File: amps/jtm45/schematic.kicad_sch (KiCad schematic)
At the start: 62 parts, among them T3 OT

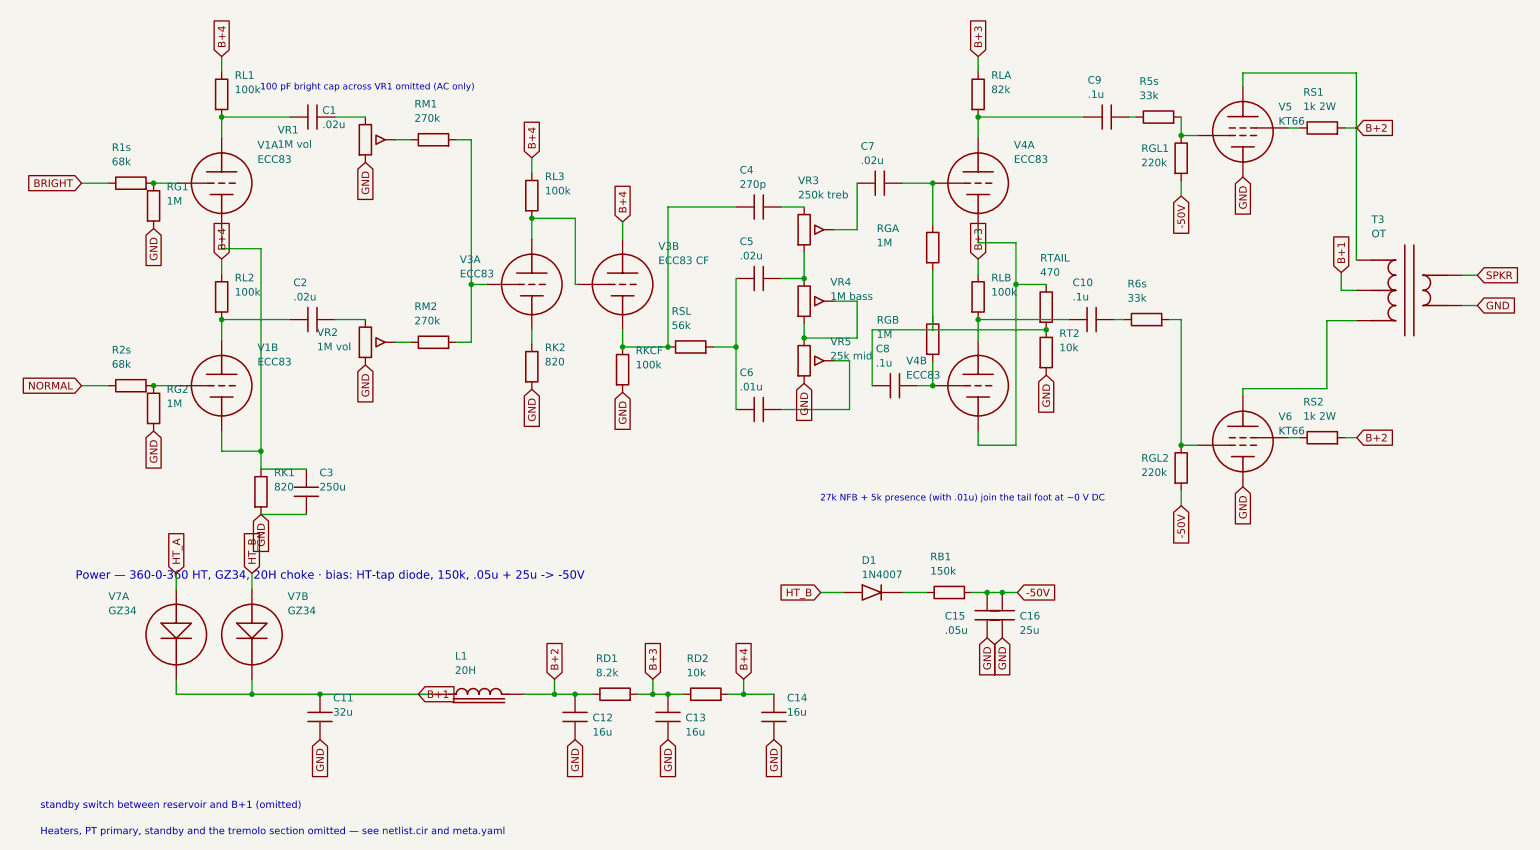
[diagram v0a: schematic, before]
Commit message: Add: real tube pin numbers and readable valve glyphs on every schematic
Phase B of the drawing program. A factory service sheet numbers every tube
pin, because the number is what a technician puts a probe on. This corpus
printed none, and the numbers hidden in its symbols were positional
placeholders (P=1, G=2, K=3) that would have published a 6V6GT's plate as
pin 1 when it is pin 3.

1055 electrodes now carry the real number, 1027 lettered (27 are shared
filaments deduped, 1 dropped for want of clear space on the 6G2). Resolved per
instance from reference/tubes/<slug>.yaml through the same alias resolution the
layout renderer uses, so a 12AX7 section and a 6SL7 section each get their own
basing. A valve whose basing the corpus does not carry prints nothing rather
than a wrong number.

Section letters and basing units are now separate things, which cost a detour
worth recording. The RCA 12AX7-A sheet reads "Pin 1 - Plate of Unit No.2 ...
Pin 6 - Plate of Unit No.1", so unit numbering is not pin order; the 5Y3 and
GZ34 number their units in opposite pin order, so nothing positional can
express it. But the section LETTER is a designator, not a basing fact: this
corpus, like every technician, calls the first stage in signal order V1A, and
five amps' prose already did. On four amps the factory sheets put that first
stage on the other half -- the AA764's own schematic prints +200 V on pin 1 --
so those drawings now state their unit explicitly, each citing its source, and
no letter, netlist, parts list or layout comment changed. 183 layout comments
agree with the printed numbers, 0 disagree. A guard fires if two halves of one
bottle resolve to the same unit, which is exactly how this was found.

Glyphs: the cathode gains a bracket and filament hairpin so it can no longer be
confused with the plate bar, the pentode's screen sits on its own row, and a
rectifier draws as one envelope over its sections instead of two apparent
bottles. Line weights are scaled per sheet to a co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
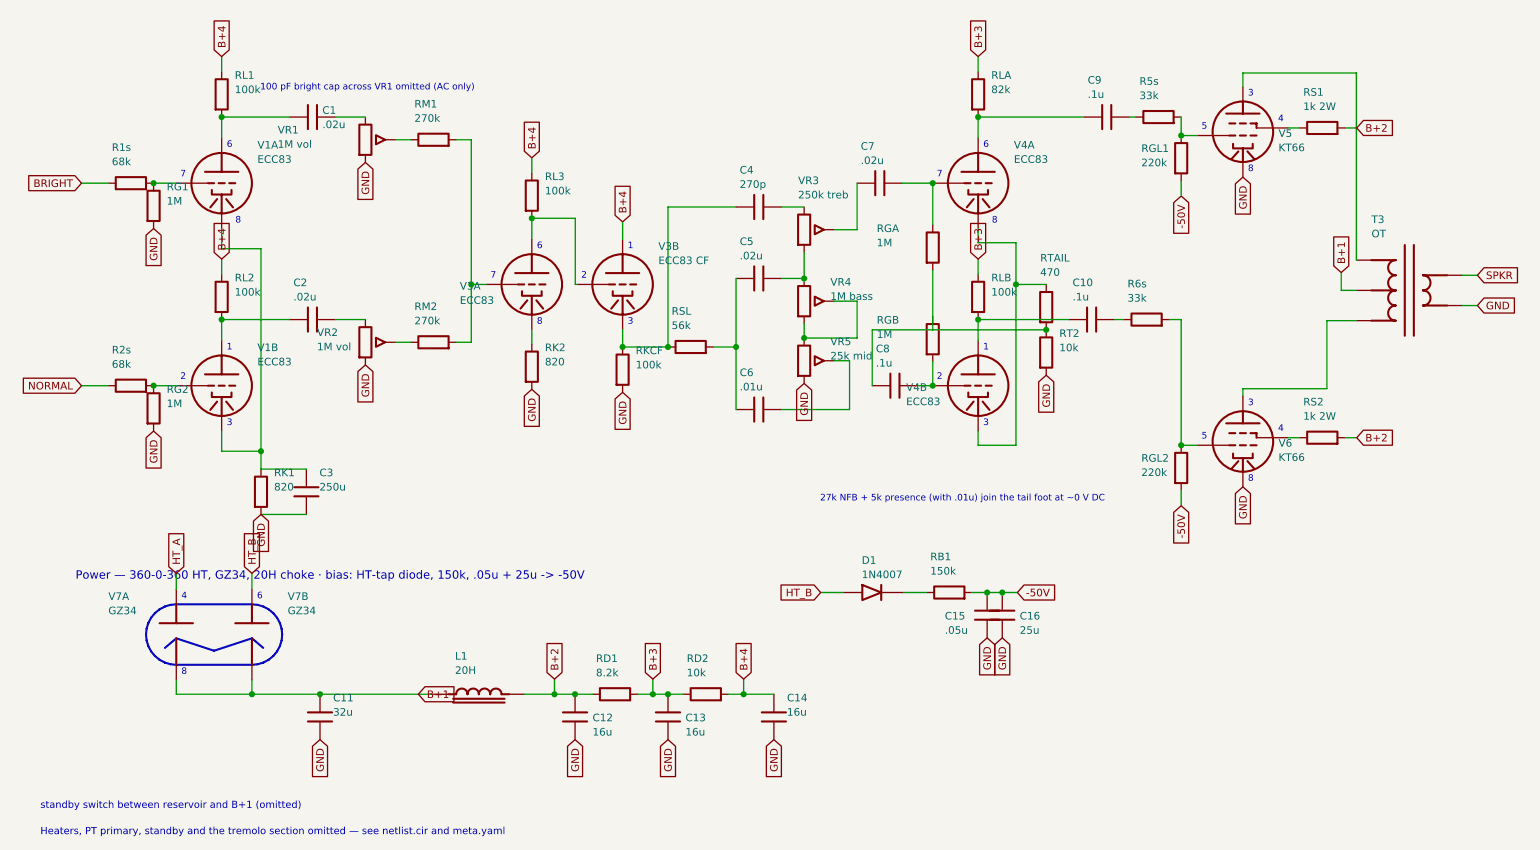
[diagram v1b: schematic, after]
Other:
- note added: "1"
- note added: "2"
- note added: "3"
- note added: "4"
- note added: "5"
- note added: "6"
- note added: "7"
- note added: "8"

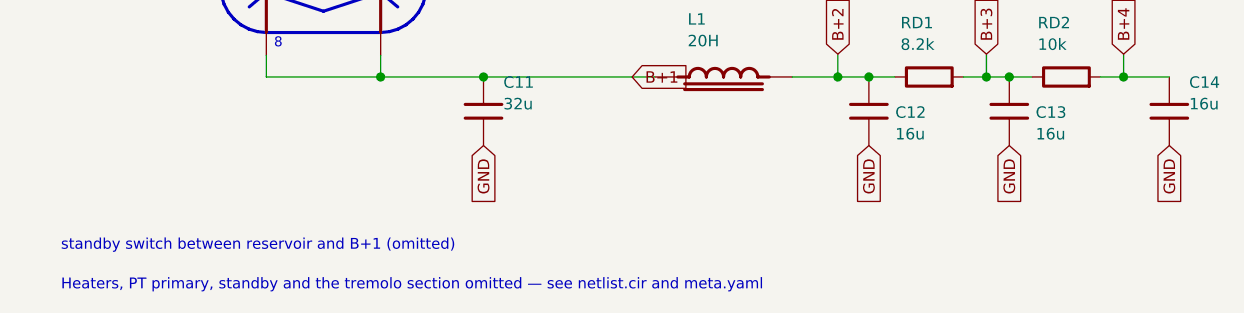
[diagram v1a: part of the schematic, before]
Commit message: Fix: schematic sheet notes no longer name repository files
Thirty-seven committed sheets rendered footnotes and section notes such as
"Heaters and PT primary omitted — see netlist.cir and meta.yaml" or
"excluded from netlist.cir (notes.md)" to visitors through KiCanvas. The
prose sweeps never counted sheets. Rewritten in the site's own words — the
netlist, the sources list, the circuit story, the parts list, the board
drawing — in 59 strings across 33 draw scripts, keeping every technical
claim as it was; the three tone sheets (6G4, 6G5, 6G6-B) are under repair
elsewhere and keep theirs for now. The sweep touched only strings passed to
the sheet's note, text, caption and footnote calls, never a path or a value.

Gates: check_schematics 40/0, connectivity 0 isolated pins;
verify_schematic_nets 40 clean; only the regenerated sheets and their served
copies changed.

Co-Authored-By: Claude Fable 5.1 <noreply@anthropic.com>
Claude-Session: https://claude.ai/code/session_01KBMfdh37HmCL2iWcBiL5J1
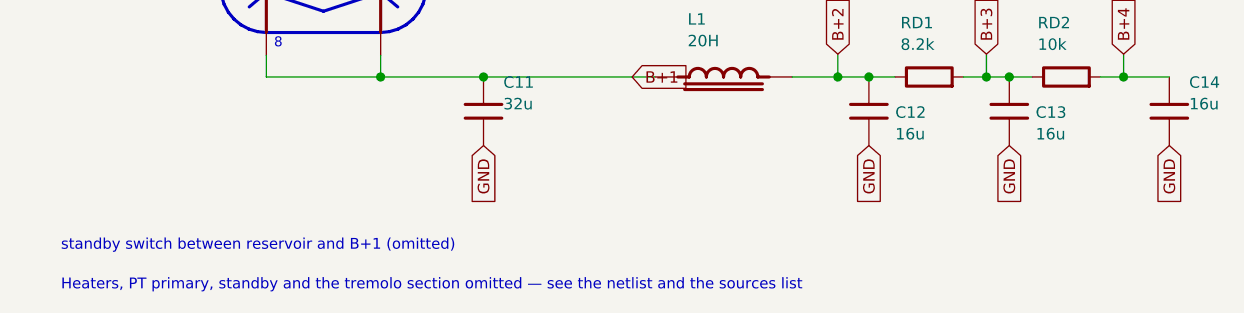
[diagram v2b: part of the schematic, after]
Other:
- note added: "Heaters, PT primary, standby and the tremolo section omitted — see the netlist and the sources list"
- note removed: "Heaters, PT primary, standby and the tremolo section omitted — see netlist.cir and meta.yaml"
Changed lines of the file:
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@@
   (text "standby switch between reservoir and B+1 (omitted)" (at 12.7 142.856 0)
     (effects (font (size 1.2 1.2)) (justify left)))
-  (text "Heaters, PT primary, standby and the tremolo section omitted — see netlist.cir and meta.yaml" (at 12.7 147.256 0)
+  (text "Heaters, PT primary, standby and the tremolo section omitted — see the netlist and the sources list" (at 12.7 147.256 0)
     (effects (font (size 1.2 1.2)) (justify left)))
   (sheet_instances (path "/" (page "1")))

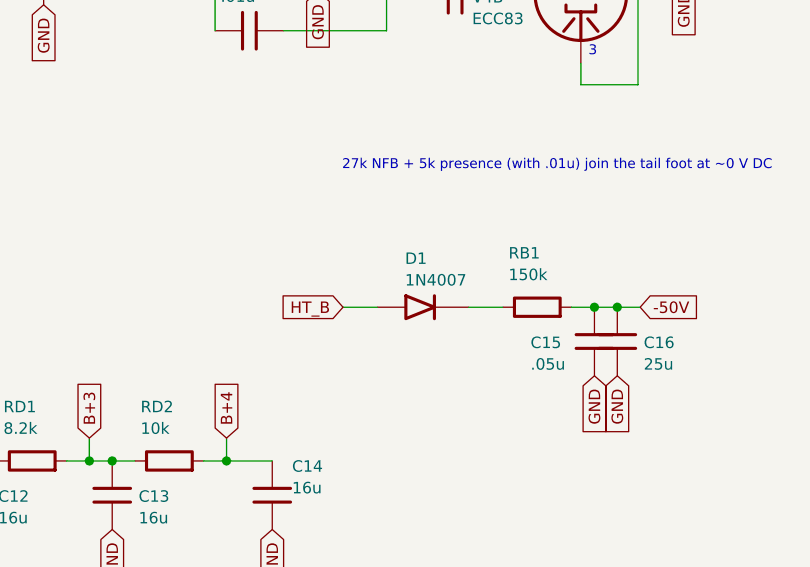
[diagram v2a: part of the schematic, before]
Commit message: Fix: 17 bias rectifiers and six HT diodes drawn backwards; the 6G6-B and 6G4 bias rows as their drawings show; AA1164 V4 units
Rectifier polarity has no gate. The netlists model every supply as an ideal
source, the sheet-vs-board check treats a two-terminal part as unordered, and
the boards' `cathode:` fields were copied from the sheets. Measured over all
68 diodes on 40 sheets: 18 negative-bias rectifiers had the cathode on the
negative node (a diode that way round would charge the node POSITIVE), and all
six 6G6-B HT diodes pointed away from B+. The printed negative bias on each of
those sheets falsifies the drawn orientation; the nine bias rectifiers already
right (AA1164, AA864, AB165, B15N, DR103, JTM100, M1959, M2204, 6G6-B) show
the idiom. Flipped: 5E4-A, 5E5-A, 5E6-A, 5F10, 5F4, 5F6, 5F6-A, 5F8-A, 5G9,
6G2, 6G3, 6G4, 6G5, AA964, AB763, AB763 Super, AB763 Twin, JTM45 (the
M1987's is with the Marshall board repair) and the 6G6-B's DR1-DR6. The
5F8-A board, which had copied its sheet, has the band moved to the tap side;
the other boards' bands are with the board-repair wave. A gate is next.

6G6-B bias. E-FB (6431x3364): the 1K 1W rises from TR1's SECOND secondary
terminal, a bias tap between the upper HT end and the grounded centre tap,
to the diode's + end. The sheet fed the diode from the HT end with the 1K
after it. T1 now carries its tap pin and the row reads tap -> 1K -> diode ->
-54 V. (The triage had read "HT end"; the native crop shows the tap.)

6G4 bias. A-FJ, read natively: tap -> rectifier -> 8 uF -> 10K -> the -55 V
node, which carries a second 8 uF and the 56K to ground as a bleeder. The
sheet fed the rectifier from an HT end, drew the 56K in series and carried
one capacitor. CBIAS2 joins the parts list, and RBIAS1's role now says
bleeder.

AA1164 V4. The K-FD sheet prints the phase inverter 7/6/8 and the tremolo
oscillator 2/1/3 (5554x4346); the sheet had them the other way round.

Gates: check_schematics 40/0 (+selftest), verify_schematic_nets 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
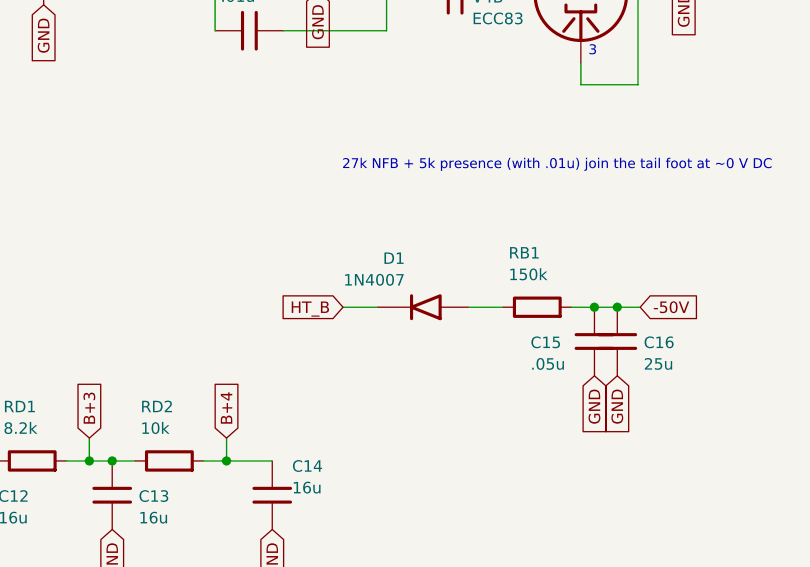
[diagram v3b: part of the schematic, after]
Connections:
- net HT_B: now also D1.2 (K); no longer D1.1 (A)
- net at RB1.1: now also D1.1 (A); no longer D1.2 (K)
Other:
- moved on the sheet: D1
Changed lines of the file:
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@@
   (wire (pts (xy 143.709 106.998) (xy 147.519 106.998))
     (stroke (width 0) (type default)))
-  (symbol (lib_id "cx:DIODE_SS") (at 152.599 106.998 0) (unit 1)
+  (symbol (lib_id "cx:DIODE_SS") (at 152.599 106.998 180) (unit 1)
     (in_bom yes) (on_board yes)
     (property "Reference" "D1" (at 150.599 101.598 0) (effects (font (size 1.27 1.27)) (justify left)))
